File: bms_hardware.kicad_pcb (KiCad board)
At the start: 2 copper layers, 150.6 x 71.7 mm, 198 parts, among them J1 Conn_01x04_Male, J2 Conn_01x07_Female, J3 Vcc In, J4 CH_TS, J5 Conn_01x05_Male, J6 DB9_Male, Q1 2N7002, Q10 FDD86580-F085, Q11 BC848, Q12 BC848, Q13 IRF9310PbF, Q2 2N7002, Q3 2N7002, Q4 2N7002, Q5 2N7002, Q6 2N7002, Q7 DMP4051LK3, Q8 DMP4051LK3, Q9 FDD86580-F085, SW1 Reset, SW2 Select CE, SW3 SW_Push, U1 ADuM1201AR, U2 BQ76PL536APAPR, U3 BQ24618RGET, U4 TPS54331D, U5 FERD2045SB-TR, U6 STM32F407VGTx, U7 PDM1-S12-S3-S, U8 SN65HVD233, U9 INA226, Y1 8MHz

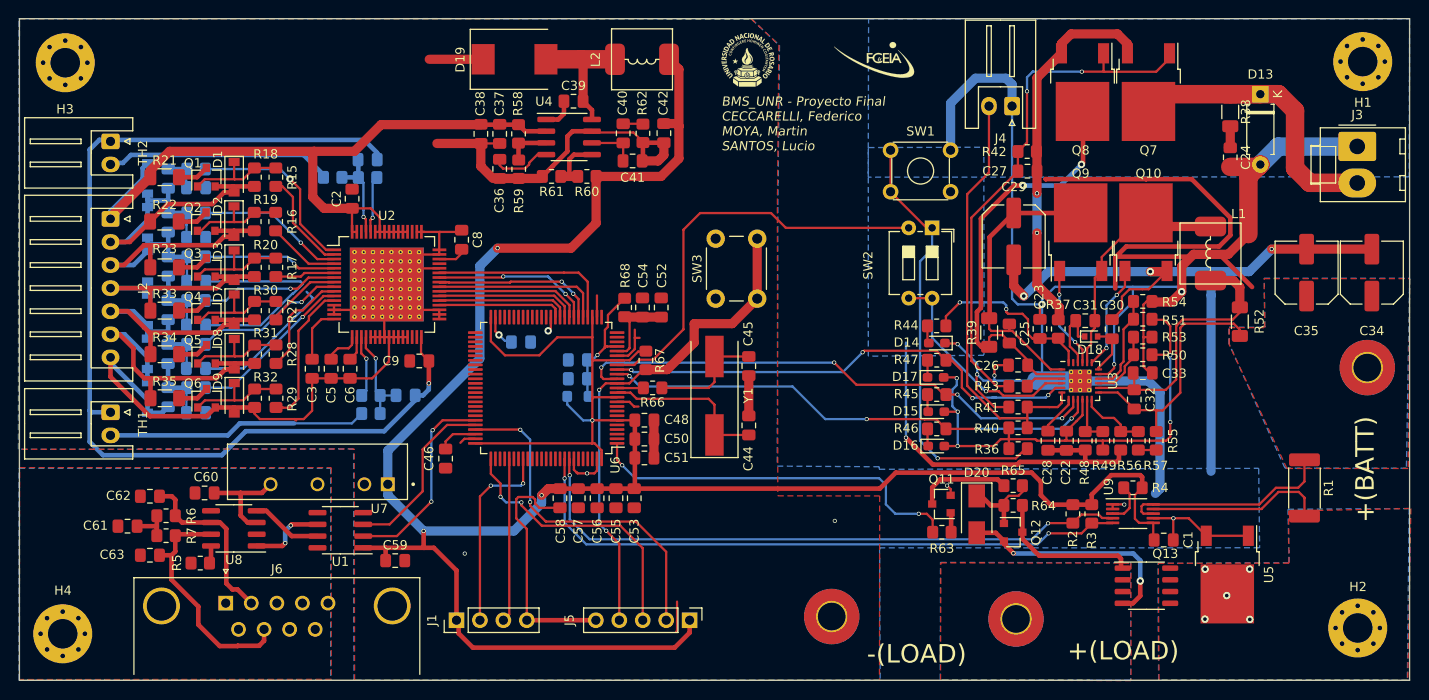
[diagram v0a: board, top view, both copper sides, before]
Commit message: Mirrors in x axis J3
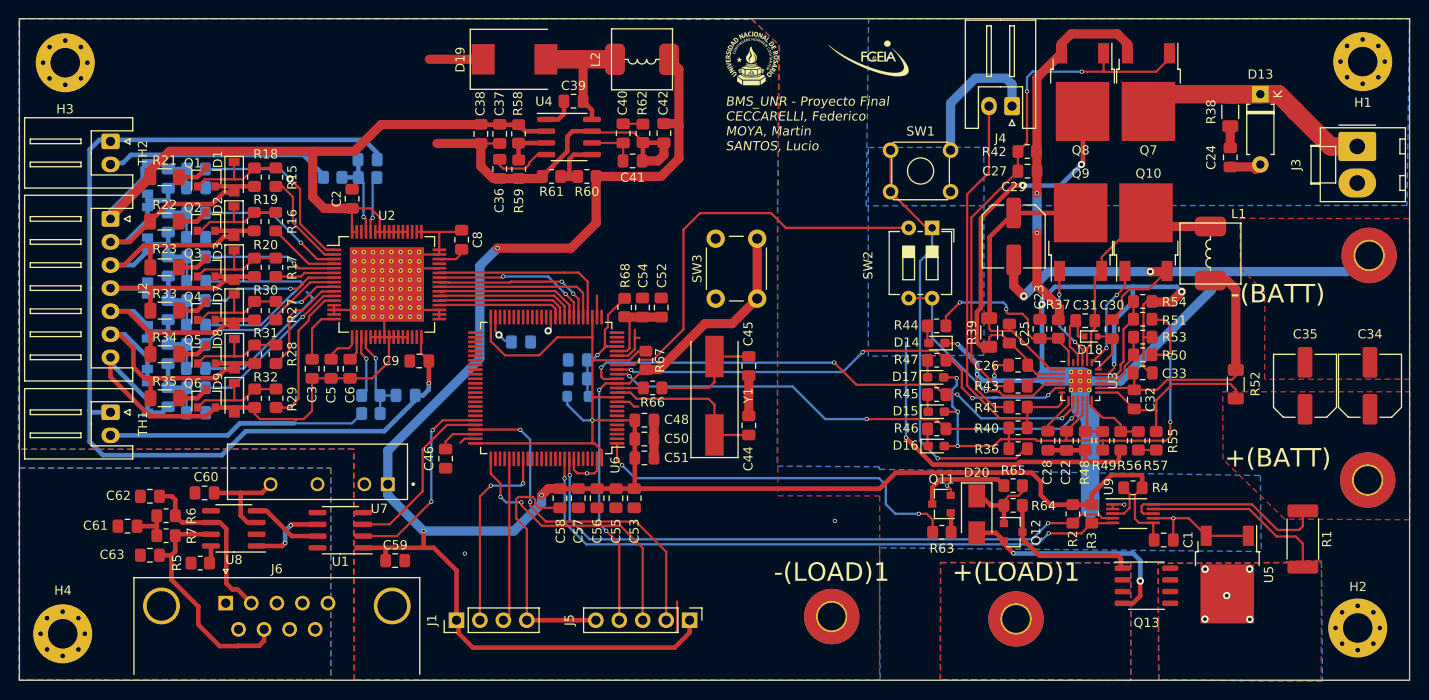
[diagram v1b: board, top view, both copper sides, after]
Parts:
- added -(BATT): MountingHole_Pad, MountingHole:MountingHole_3mm_Pad_TopBottom, F.Cu at (231.8, 107.2)
- moved C34 12.3 mm to (231.9, 121.3)
- moved C35 12.3 mm to (224.9, 121.3)
- moved +(BATT) 12.2 mm to (231.7, 131.5)
- moved R52 6.79 mm to (217.4, 121.1)
- moved R1 5.53 mm to (224.6, 137.9)
- moved NT1 1.16 mm to (198.8, 120.3)
- moved G*** 0.61 mm to (177.5, 86.0)
- moved G*** 0.47 mm to (165.0, 85.8)
- renumbered +(LOAD) to +(LOAD)1, -(LOAD) to -(LOAD)1
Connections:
- J3 pad 1: GND1 -> Net-(D13-Pad1)
- J3 pad 2: Net-(D13-Pad1) -> GND1
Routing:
- net GND1: track 246.5 -> 136.9 mm
- net GND: track 353.6 -> 345.7 mm, vias 10 -> 9
- net +BATT: track 50.4 -> 43.7 mm
- net Net-(D13-Pad1): track 34.9 -> 29.7 mm
- net NRST: track 54.8 -> 53.6 mm
- net /bat_switch/D: track 19.4 -> 20.3 mm
- removed copper zone on B.Cu, net +BATT
